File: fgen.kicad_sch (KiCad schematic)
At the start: 13 parts

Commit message: first draft
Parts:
- removed R?: (no value), symbol Device:R_US
- removed U?: (no value), symbol Regulator_Linear:LM79M05_TO220
- removed U?: (no value), symbol Regulator_Linear:L78L05_TO92
- added D3, D4: 15V, symbol Device:D_Zener
- added J2: (no value), symbol Connector:Conn_01x02_Female
- added Q1: TIP29C, Package_TO_SOT_THT:TO-220-3_Vertical, symbol Device:Q_NPN_BCE
- added Q2: TIP30C, symbol Device:Q_PNP_BCE
- added Q3: 2N3904, Package_TO_SOT_THT:TO-92_Inline, symbol Transistor_BJT:2N3904
- added Q4: 2N3906, Package_TO_SOT_THT:TO-92_Inline, symbol Transistor_BJT:2N3906
- added R4: 10k, symbol Device:R_US
- C1: renamed from C?; value (none) -> 680uF
- D1: renamed from D?; value (none) -> 1N4004; footprint (none) -> Diode_THT:D_DO-41_SOD81_P10.16mm_Horizontal
- J1: renamed from J?; value (none) -> AudioPlug3
- R1: renamed from R?; value (none) -> 22k
- R2: renamed from R?; value (none) -> 180k
- R3: renamed from R?; value (none) -> 10k
- T1: renamed from T?; value (none) -> Transformer_1P_1S
- U1: renamed from U?; value (none) -> LM741
- gave numbers to parts that had none: 2
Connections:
- net +15V: now also Q3.1 (E)
- net +VDC: now also R3.1, Q1.2 (C), Q3.3 (C)
- net -15V: now also Q4.1 (E)
- net -VDC: now also Q2.2 (C), Q4.2 (B), R4.2
- net GND: now also D3.2 (A), D4.1 (K), J2.2 (Pin_2)
- net at R3.2: now also D3.1 (K), Q3.2 (B)
- net at U1.6: now also Q1.1 (B), Q2.1 (B)
- net Vout: now reaches R2.2
- net Vout: now also J2.1 (Pin_1), Q1.3 (E), Q2.3 (E)
- new net: D4.2 (A), Q4.3 (C), R4.1
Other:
- note added: "10:1 amplification"
- moved on the sheet: J1, R1, R2, R3, U1

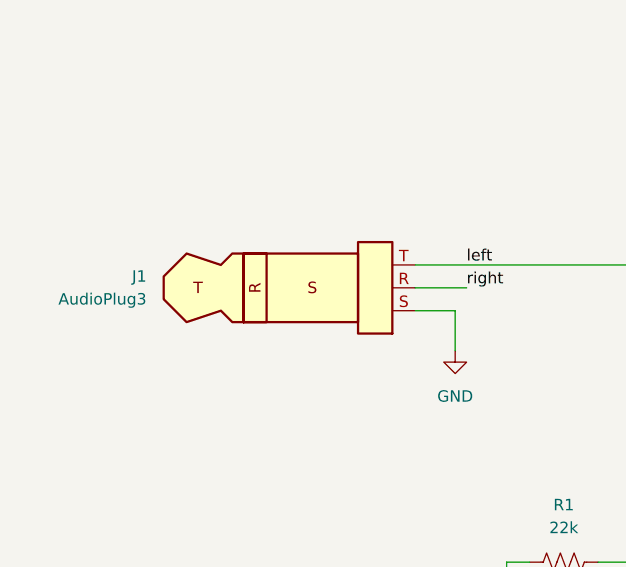
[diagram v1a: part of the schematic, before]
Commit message: Breadboard layout done
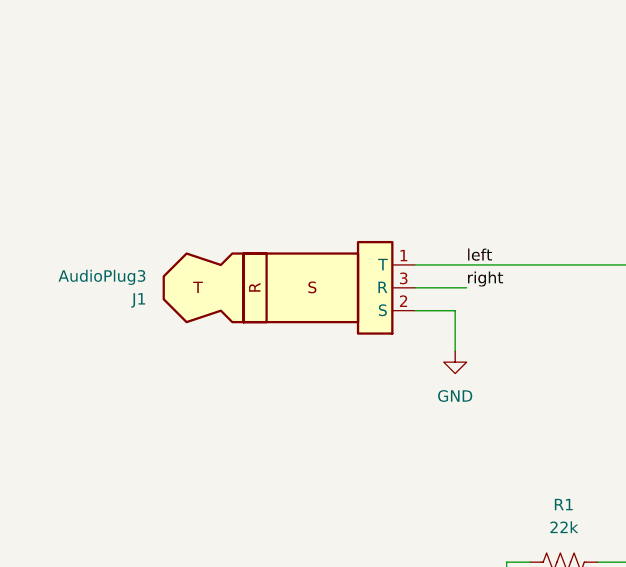
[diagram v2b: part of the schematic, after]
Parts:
- J1: footprint (none) -> Connector_PinHeader_2.54mm:PinHeader_1x03_P2.54mm_Vertical
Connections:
- net GND: now also J1.2 (S); no longer J1.S
- net left: now also J1.1 (T); no longer J1.T
- net right: now also J1.3 (R); no longer J1.R
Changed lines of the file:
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@@
   (symbol (lib_id "Connector:AudioPlug3") (at 62.23 116.84 0) (mirror x) (unit 1)
     (in_bom yes) (on_board yes) (fields_autoplaced)
-    (property "Reference" "J1" (id 0) (at 47.625 115.5699 0)
+    (property "Reference" "J1" (id 0) (at 47.625 118.1101 0)
       (effects (font (size 1.27 1.27)) (justify right))
     )
-    (property "Value" "AudioPlug3" (id 1) (at 47.625 118.1099 0)
+    (property "Value" "AudioPlug3" (id 1) (at 47.625 115.5701 0)
       (effects (font (size 1.27 1.27)) (justify right))
     )
-    (property "Footprint" "" (id 2) (at 64.77 115.57 0)
+    (property "Footprint" "Connector_PinHeader_2.54mm:PinHeader_1x03_P2.54mm_Vertical" (id 2) (at 64.77 118.11 0)
       (effects (font (size 1.27 1.27)) hide)
     )
-    (property "Datasheet" "~" (id 3) (at 64.77 115.57 0)
+    (property "Datasheet" "~" (id 3) (at 64.77 118.11 0)
       (effects (font (size 1.27 1.27)) hide)
     )
-    (pin "R")
-    (pin "S")
-    (pin "T")
+    (pin "1")
+    (pin "2")
+    (pin "3")
   )
   (symbol (lib_id "Connector:Conn_01x02_Female") (at 167.64 119.38 0) (unit 1)

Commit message: schematic bug fix
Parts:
- R1: value 22k -> (none)
- R2: value 180k -> (none)
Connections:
- net -VDC: now also Q4.3 (C); no longer Q4.2 (B)
- net at D4.2 (A), R4.1: now also Q4.2 (B); no longer Q4.3 (C)
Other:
- note added: "100:1 amplification"
- note removed: "10:1 amplification"
- moved on the sheet: Q4
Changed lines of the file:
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@@
+    (stroke (width 0) (type default) (color 0 0 0 0))
+  )
+  (wire (pts (xy 134.62 82.55) (xy 128.27 82.55))
     (stroke (width 0) (type default) (color 0 0 0 0))
   )
@@
     (stroke (width 0) (type default) (color 0 0 0 0))
   )
+  (wire (pts (xy 139.7 72.39) (xy 139.7 74.93))
+    (stroke (width 0) (type default) (color 0 0 0 0))
+  )
   (wire (pts (xy 128.27 36.83) (xy 128.27 38.1))
     (stroke (width 0) (type default) (color 0 0 0 0))
@@
     (stroke (width 0) (type default) (color 0 0 0 0))
   )
-  (wire (pts (xy 139.7 80.01) (xy 139.7 82.55))
-    (stroke (width 0) (type default) (color 0 0 0 0))
-  )
   (wire (pts (xy 135.89 118.11) (xy 135.89 119.38))
     (stroke (width 0) (type default) (color 0 0 0 0))
@@
     (stroke (width 0) (type default) (color 0 0 0 0))
   )
-  (wire (pts (xy 144.78 72.39) (xy 149.86 72.39))
+  (wire (pts (xy 144.78 82.55) (xy 149.86 82.55))
     (stroke (width 0) (type default) (color 0 0 0 0))
   )
@@
     (stroke (width 0) (type default) (color 0 0 0 0))
   )
-  (wire (pts (xy 128.27 72.39) (xy 134.62 72.39))
+  (wire (pts (xy 128.27 72.39) (xy 139.7 72.39))
     (stroke (width 0) (type default) (color 0 0 0 0))
   )
@@
     (stroke (width 0) (type default) (color 0 0 0 0))
   )
-  (wire (pts (xy 149.86 72.39) (xy 149.86 69.85))
+  (wire (pts (xy 149.86 82.55) (xy 149.86 80.01))
     (stroke (width 0) (type default) (color 0 0 0 0))
   )
@@
     (stroke (width 0) (type default) (color 0 0 0 0))
   )
-  (wire (pts (xy 139.7 82.55) (xy 128.27 82.55))
-    (stroke (width 0) (type default) (color 0 0 0 0))
-  )
   (wire (pts (xy 128.27 71.12) (xy 128.27 72.39))
     (stroke (width 0) (type default) (color 0 0 0 0))
@@
     (stroke (width 0) (type default) (color 0 0 0 0))
   )
-  (text "10:1 amplification" (at 96.52 152.4 0)
+  (text "100:1 amplification" (at 96.52 152.4 0)
     (effects (font (size 1.27 1.27)) (justify left bottom))
   )
@@
     (pin "1")
   )
-  (symbol (lib_id "Transistor_BJT:2N3906") (at 139.7 74.93 90) (unit 1)
-    (in_bom yes) (on_board yes) (fields_autoplaced)
-    (property "Reference" "Q4" (id 0) (at 139.7 66.04 90))
-    (property "Value" "2N3906" (id 1) (at 139.7 68.58 90))
-    (property "Footprint" "Package_TO_SOT_THT:TO-92_Inline" (id 2) (at 141.605 69.85 0)
+  (symbol (lib_id "Transistor_BJT:2N3906") (at 139.7 80.01 90) (mirror x) (unit 1)
+    (in_bom yes) (on_board yes) (fields_autoplaced)
+    (property "Reference" "Q4" (id 0) (at 139.7 86.36 90))
+    (property "Value" "2N3906" (id 1) (at 139.7 88.9 90))
+    (property "Footprint" "Package_TO_SOT_THT:TO-92_Inline" (id 2) (at 141.605 85.09 0)
       (effects (font (size 1.27 1.27) italic) (justify left) hide)
     )
-    (property "Datasheet" "https://www.onsemi.com/pub/Collateral/2N3906-D.PDF" (id 3) (at 139.7 74.93 0)
+    (property "Datasheet" "https://www.onsemi.com/pub/Collateral/2N3906-D.PDF" (id 3) (at 139.7 80.01 0)
       (effects (font (size 1.27 1.27)) (justify left) hide)
     )
@@
     (in_bom yes) (on_board yes) (fields_autoplaced)
     (property "Reference" "R1" (id 0) (at 93.98 140.97 90))
-    (property "Value" "22k" (id 1) (at 93.98 143.51 90))
+    (property "Value" "" (id 1) (at 93.98 143.51 90))
     (property "Footprint" "" (id 2) (at 94.234 146.304 90)
       (effects (font (size 1.27 1.27)) hide)
@@
     (pin "1")
   )
-  (symbol (lib_id "power:-15V") (at 149.86 69.85 0) (unit 1)
-    (in_bom yes) (on_board yes) (fields_autoplaced)
-    (property "Reference" "#PWR0117" (id 0) (at 149.86 67.31 0)
-      (effects (font (size 1.27 1.27)) hide)
-    )
-    (property "Value" "-15V" (id 1) (at 149.86 64.77 0))
-    (property "Footprint" "" (id 2) (at 149.86 69.85 0)
-      (effects (font (size 1.27 1.27)) hide)
-    )
-    (property "Datasheet" "" (id 3) (at 149.86 69.85 0)
+  (symbol (lib_id "power:-15V") (at 149.86 80.01 0) (unit 1)
+    (in_bom yes) (on_board yes) (fields_autoplaced)
+    (property "Reference" "#PWR0117" (id 0) (at 149.86 77.47 0)
+      (effects (font (size 1.27 1.27)) hide)
+    )
+    (property "Value" "-15V" (id 1) (at 149.86 74.93 0))
+    (property "Footprint" "" (id 2) (at 149.86 80.01 0)
+      (effects (font (size 1.27 1.27)) hide)
+    )
+    (property "Datasheet" "" (id 3) (at 149.86 80.01 0)
       (effects (font (size 1.27 1.27)) hide)
     )
@@
     (in_bom yes) (on_board yes) (fields_autoplaced)
     (property "Reference" "R2" (id 0) (at 115.57 140.97 90))
-    (property "Value" "180k" (id 1) (at 115.57 143.51 90))
+    (property "Value" "" (id 1) (at 115.57 143.51 90))
     (property "Footprint" "" (id 2) (at 115.824 146.304 90)
       (effects (font (size 1.27 1.27)) hide)
@@
     )
     (path "/c657675e-8deb-40bb-80e5-5beec789b8d6"
-      (reference "R1") (unit 1) (value "22k") (footprint "Resistor_THT:R_Axial_DIN0204_L3.6mm_D1.6mm_P5.08mm_Horizontal")
+      (reference "R1") (unit 1) (value "1k") (footprint "Resistor_THT:R_Axial_DIN0204_L3.6mm_D1.6mm_P5.08mm_Horizontal")
     )
     (path "/d52775ee-dd56-474f-8b5c-c66029880e5c"
-      (reference "R2") (unit 1) (value "180k") (footprint "Resistor_THT:R_Axial_DIN0204_L3.6mm_D1.6mm_P5.08mm_Horizontal")
+      (reference "R2") (unit 1) (value "100k") (footprint "Resistor_THT:R_Axial_DIN0204_L3.6mm_D1.6mm_P5.08mm_Horizontal")
     )
     (path "/0730ab8b-8800-4efd-8a32-32110996c7a0"

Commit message: Prototyped on breadboard, updated gain resistor
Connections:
- net fb: now reaches R1.2, R2.1, U1.2 (-)
- net ctrl: now reaches Q1.1 (B), Q2.1 (B), U1.6
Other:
- note added: "20V peak-to-peak at full amplitude"
- note removed: "100:1 amplification"
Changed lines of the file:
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@@
     (stroke (width 0) (type default) (color 0 0 0 0))
   )
-  (text "100:1 amplification" (at 96.52 152.4 0)
+  (text "20V peak-to-peak at full amplitude" (at 96.52 152.4 0)
     (effects (font (size 1.27 1.27)) (justify left bottom))
   )
@@
   )
   (label "left" (at 83.185 114.3 0)
+    (effects (font (size 1.27 1.27)) (justify left bottom))
+  )
+  (label "fb" (at 101.6 135.89 0)
+    (effects (font (size 1.27 1.27)) (justify left bottom))
+  )
+  (label "ctrl" (at 119.38 116.84 0)
     (effects (font (size 1.27 1.27)) (justify left bottom))
   )
@@
     )
     (path "/c657675e-8deb-40bb-80e5-5beec789b8d6"
-      (reference "R1") (unit 1) (value "1k") (footprint "Resistor_THT:R_Axial_DIN0204_L3.6mm_D1.6mm_P5.08mm_Horizontal")
+      (reference "R1") (unit 1) (value "470") (footprint "Resistor_THT:R_Axial_DIN0204_L3.6mm_D1.6mm_P5.08mm_Horizontal")
     )
     (path "/d52775ee-dd56-474f-8b5c-c66029880e5c"
